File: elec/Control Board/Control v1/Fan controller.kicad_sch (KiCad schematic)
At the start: 30 parts, among them J10 Conn_01x05, J11 Conn_01x04, J12 Conn_01x07, J13 Screw_Terminal_01x02, J21 Conn_01x04_Pin, J6 DB25_Female_MountingHoles, J9 Conn_01x04, Q12 NCE01P30K, Q601 BSS138

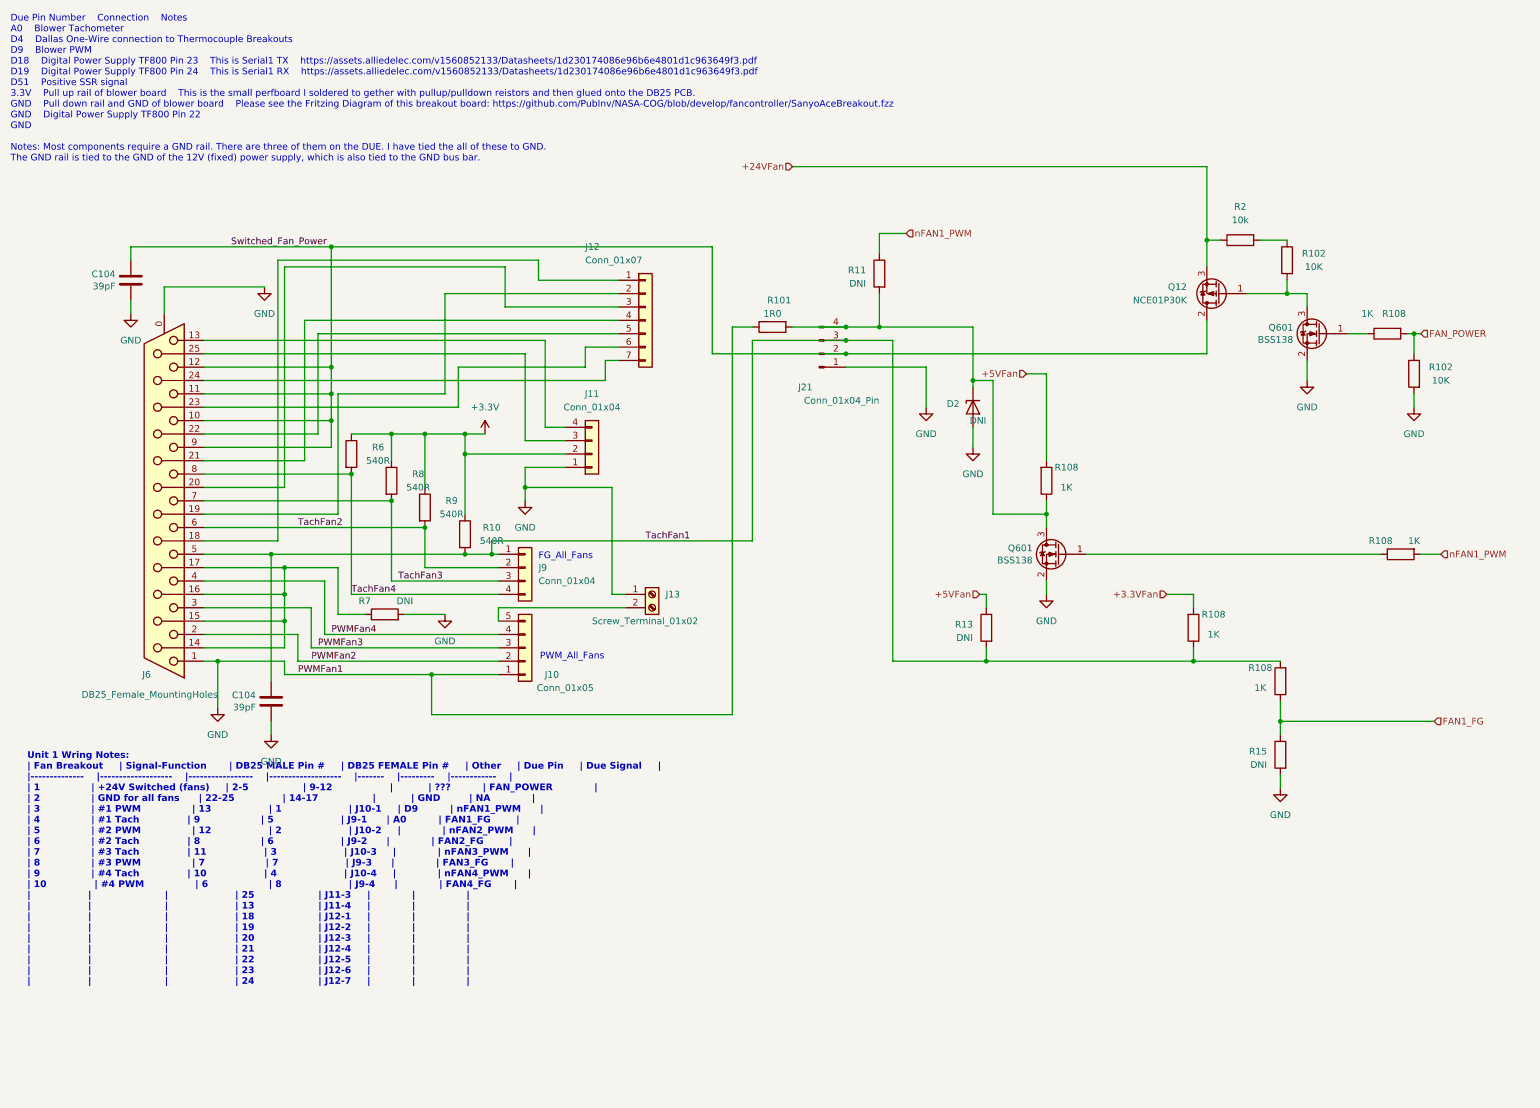
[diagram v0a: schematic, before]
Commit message: Add fan circuits. Add thermocouple interface circuits.
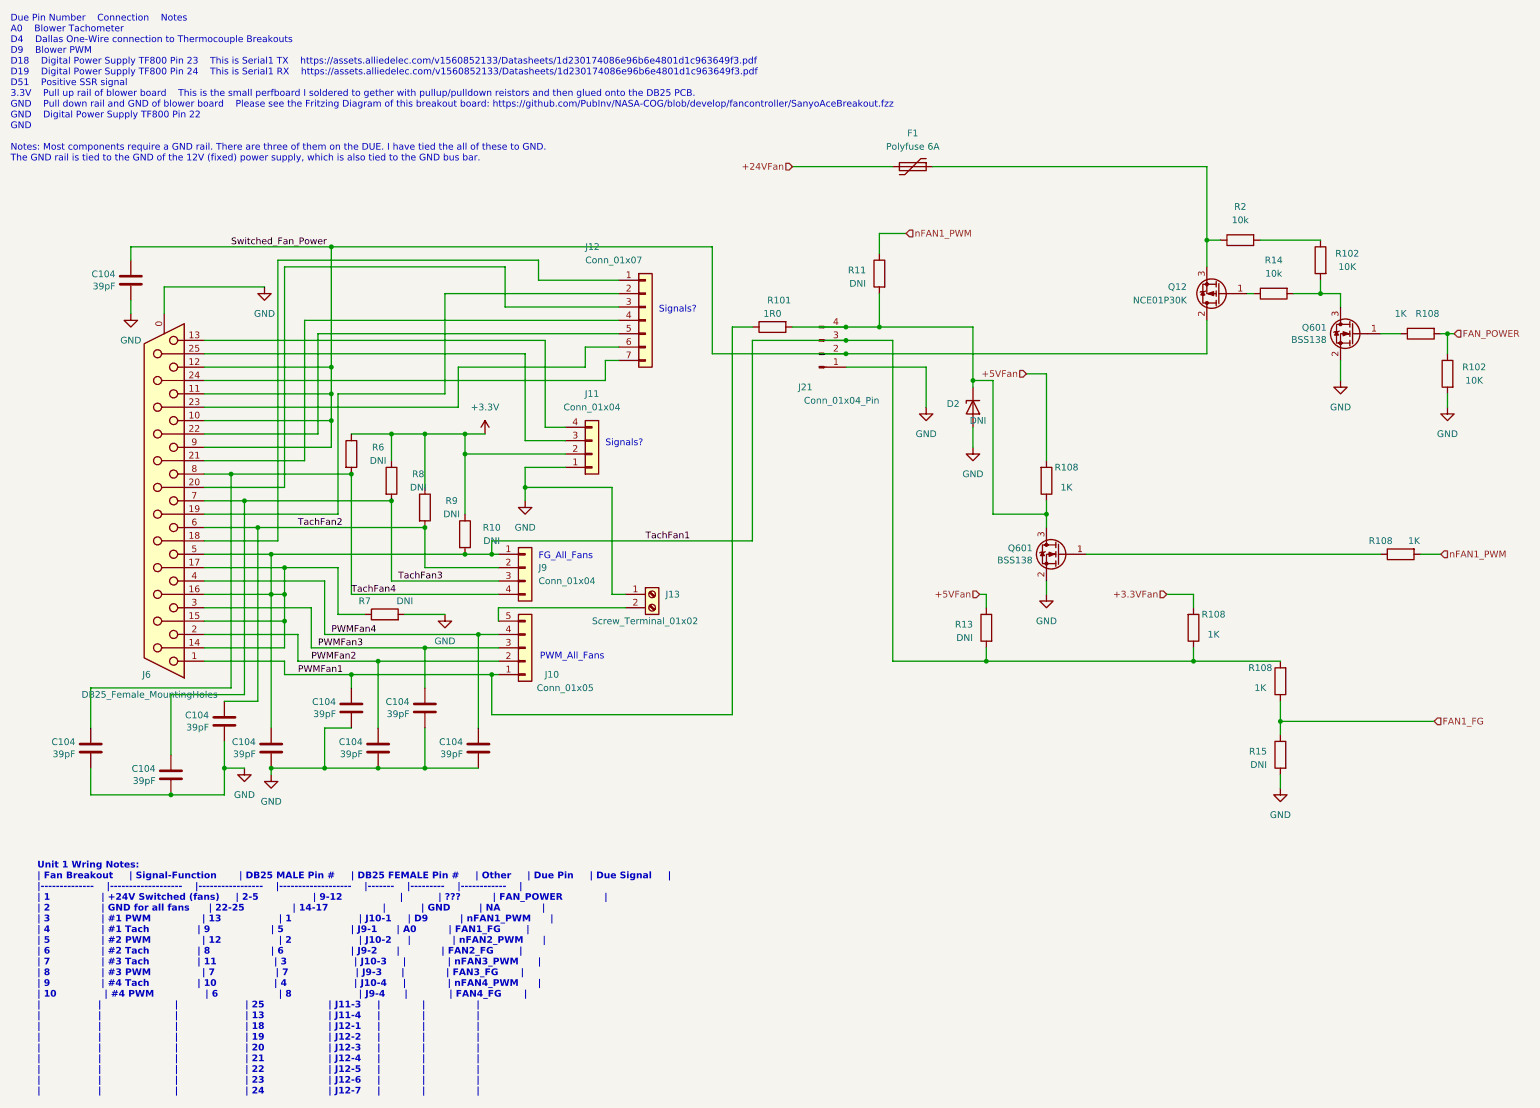
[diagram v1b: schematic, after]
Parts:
- added C104 (x7): 39pF, Capacitor_SMD:C_0603_1608Metric_Pad1.08x0.95mm_HandSolder, symbol Device:C
- added F1: Polyfuse 6A, GeneralPurposeAlarmDevicePCB:PlaceHolderOpossum, symbol Device:Polyfuse
- added R14: 10k, symbol Device:R
- R10, R6, R8, R9: value 540R -> DNI
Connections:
- net +24VFan: now also F1.2; no longer Q12.3 (S), R2.1
- net GND: now also C104.2, C104.2, C104.2, C104.2, C104.2, C104.2, C104.2; no longer J10.1 (Pin_1), J6.1, R101.1
- net PWMFan2: now also C104.1
- net PWMFan3: now also C104.1
- net PWMFan4: now also C104.1
- net TachFan1: now also J6.14 (P14), J6.15 (P15), J6.16 (P16), J6.17 (P17), R7.1
- net TachFan2: now also C104.1
- net TachFan3: now also C104.1
- net TachFan4: now also C104.1
- net at Q601.3 (D), R102.2: now also R14.2; no longer Q12.1 (G)
- new net: F1.1, Q12.3 (S), R2.1
- new net: Q12.1 (G), R14.1
- new net PWMFan1: C104.1, J10.1 (Pin_1), J6.1, R101.1
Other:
- note added: "Signals?"
- moved on the sheet: C104, Q601, R102, R108

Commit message: Move some components for rough placement.
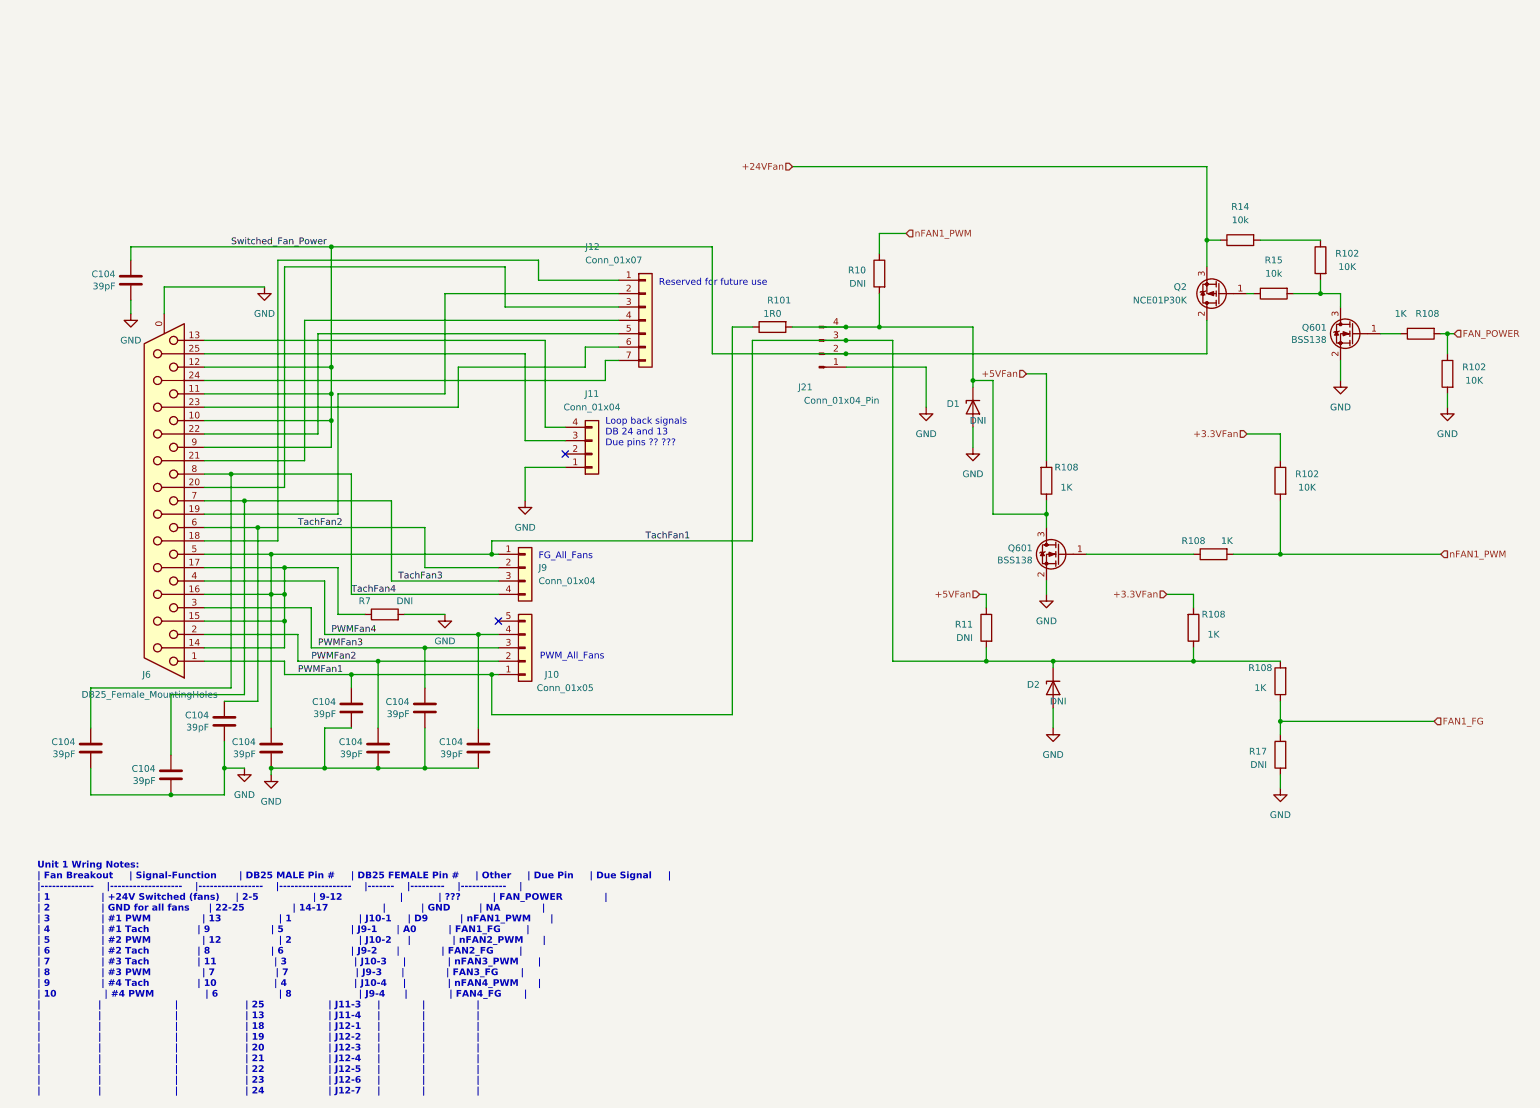
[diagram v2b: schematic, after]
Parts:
- removed F1: Polyfuse 6A, GeneralPurposeAlarmDevicePCB:PlaceHolderOpossum, symbol Device:Polyfuse
- removed J13: Screw_Terminal_01x02, TerminalBlock_MetzConnect:TerminalBlock_MetzConnect_Type073_RT02602HBLU_1x02_P5.08mm_Horizontal, symbol Connector:Screw_Terminal_01x02
- removed R10, R6, R8, R9: DNI, Resistor_SMD:R_0603_1608Metric_Pad0.98x0.95mm_HandSolder, symbol Device:R
- added D2: DNI, Diode_SMD:D_MiniMELF, symbol Diode:BZV55B3V3
- added R102: 10K, Resistor_SMD:R_0603_1608Metric_Pad0.98x0.95mm_HandSolder, symbol Device:R
- D1: renamed from D2; AssemblyType (none) -> SMT
- J21: footprint (none) -> Connector_PinHeader_2.54mm:PinHeader_1x04_P2.54mm_Vertical
- renumbered Q12 to Q2, R11 to R10, R13 to R11, R2 to R14, R14 to R15, R15 to R17
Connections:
- net +24VFan: now also Q2.3 (S), R14.1
- net +3.3VFan: now also R102.1
- net GND: now also D2.2 (A)
- net TachFan1: now also D2.1 (K)
- net nFAN1_PWM: now also R102.2
- net +3.3V: no longer names the net of J11.2 (Pin_2)
- no-connect marks 0 -> 2
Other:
- note added: "Loop back signals DB 24 and 13 Due pins ?? ???"
- note added: "Reserved for future use"
- note removed: "Due Pin Number Connection Notes A0 Blower Tachometer D4 Dallas One-Wire connection to Thermocouple Breakouts D9 Blower PWM D18 Digital Power Supply TF800 Pin 23 This is Serial1 TX https://assets.alliedelec.com/v1560852133/Datasheets/1d230174086e96b6e4801d1c963649f3.pdf D19 Digital Power Supply TF800 Pin 24 This is Serial1 RX https://assets.alliedelec.com/v1560852133/Datasheets/1d230174086e96b6e48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"
- note removed: "Signals?"

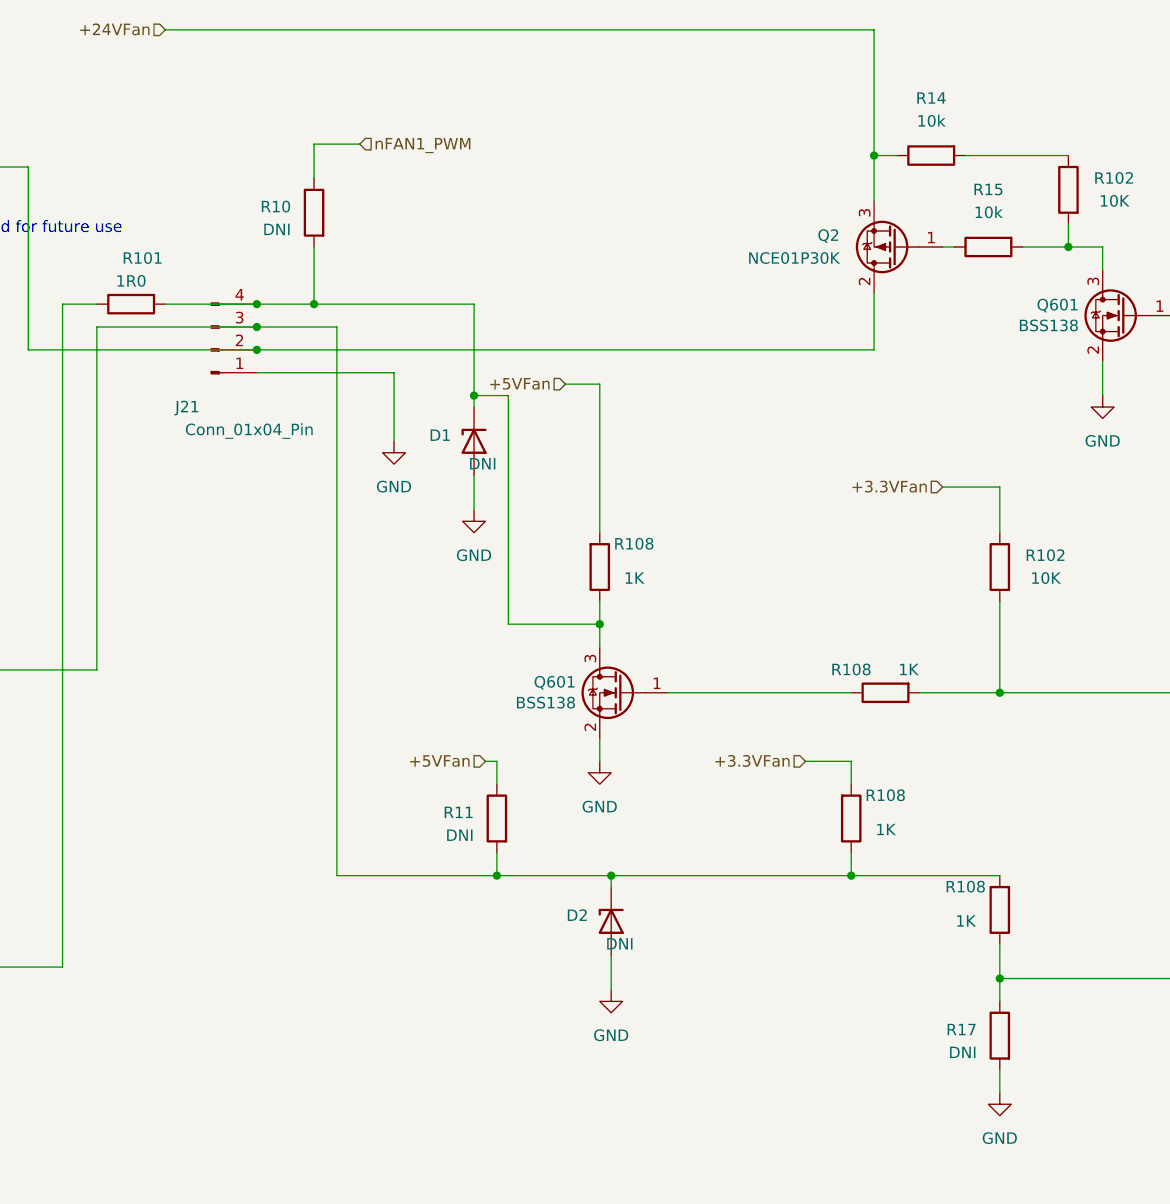
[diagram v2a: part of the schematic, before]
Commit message: Add footrpint to Max31850 module.
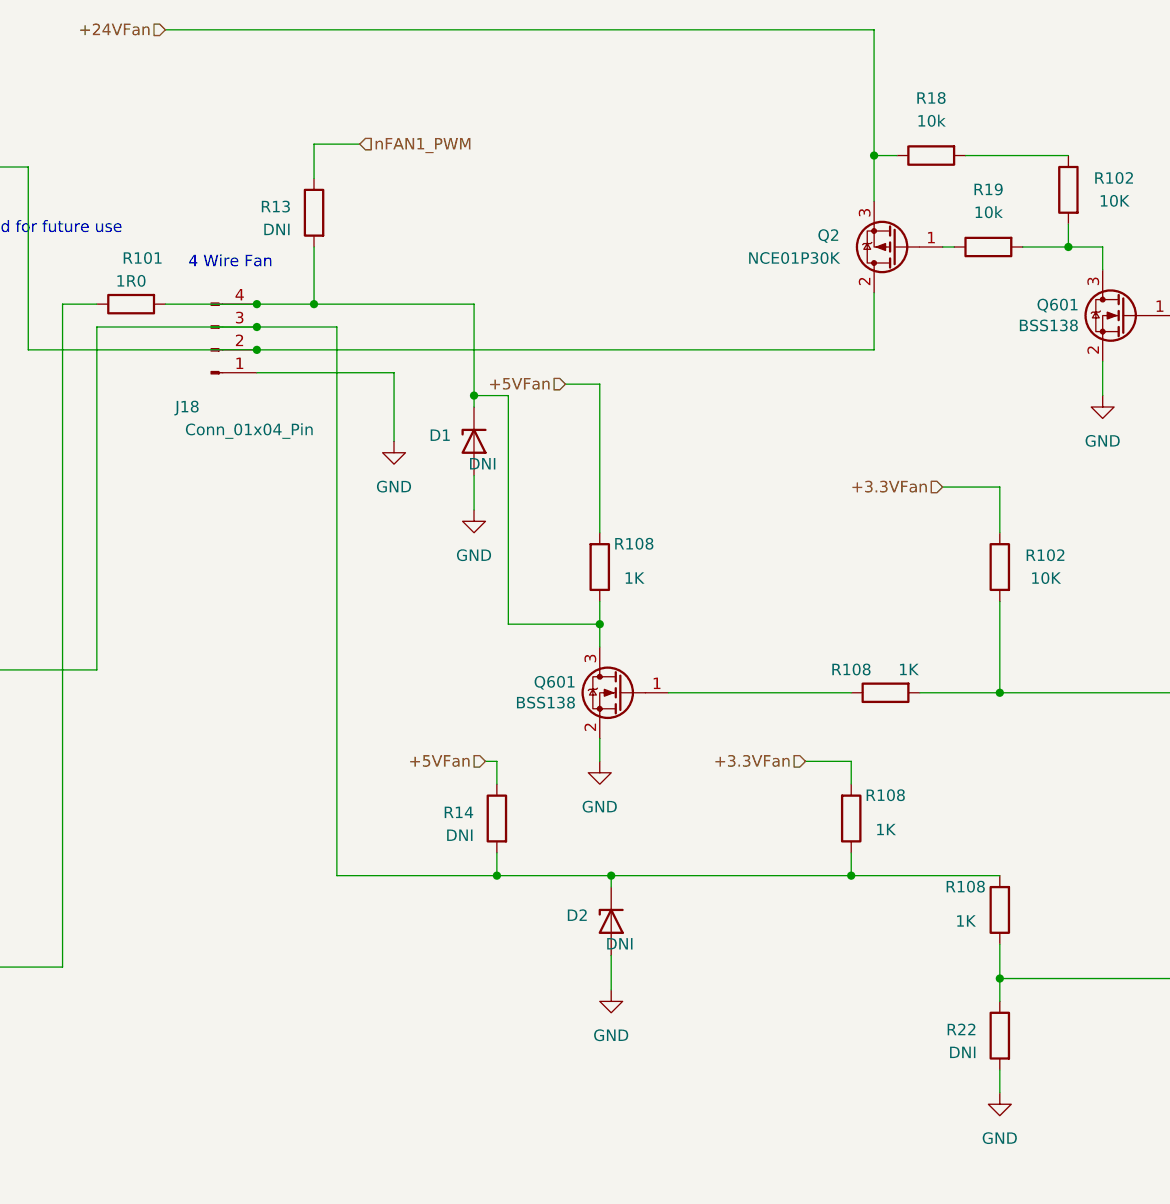
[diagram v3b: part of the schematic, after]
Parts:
- renumbered J21 to J18, R10 to R13, R11 to R14, R14 to R18, R15 to R19, R17 to R22
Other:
- note added: "4 Wire Fan"
